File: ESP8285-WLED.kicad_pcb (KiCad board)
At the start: 2 copper layers, 62.2 x 35.6 mm, 56 parts, among them J1 WLED, J2 USB_B_Micro, J3 ANT, Q1 UMH3N, SW1 RESET, SW2 FLASH, U1 ME3116, U2 ESP8285, U3 ME6211, U4 TXS0101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

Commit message: more tweaking
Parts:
- moved C1 2.58 mm to (126.5, 117.1), turned to 270 degrees
- moved R16 2.51 mm to (141.4, 113.5)
- moved C2 2.29 mm to (132.2, 117.2), turned to 270 degrees
- moved Y1 1.19 mm to (129.3, 117.2), turned to 0 degrees
- moved R7 0.59 mm to (127.4, 114.6)
- moved R15 0.34 mm to (141.0, 114.7), turned to 315 degrees
- turned SW1 to 0 degrees
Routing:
- net /RST: track 42.7 -> 34.7 mm, vias 0 -> 2
- net +3V3: track 130.9 -> 137.5 mm
- net GND: track 16.8 -> 12.5 mm, vias 54 -> 58
- net Net-(C15-Pad1): track 4.42 -> 1.99 mm
- net Net-(AE1-Pad1): track 1.86 -> 4.25 mm
- net /XI: track 6.90 -> 5.43 mm
- net /CUTXD: track 19.1 -> 20.5 mm
- net /XO: track 6.88 -> 7.95 mm
- net /UTXD: track 3.43 -> 2.79 mm

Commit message: even more tweaks
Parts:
- moved H1 0.19 mm to (149.3, 123.8)
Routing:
- net Net-(J2-Pad6): track 12.7 -> 19.1 mm
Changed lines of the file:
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@@
     (thickness 1.6)
     (drawings 14)
-    (tracks 441)
+    (tracks 447)
     (zones 0)
     (modules 56)
@@
   )
   (setup
-    (last_trace_width 0.25)
+    (last_trace_width 0.9)
     (user_trace_width 0.35)
     (user_trace_width 0.5)
@@
   )
   (module MountingHole:MountingHole_4mm (layer F.Cu)
-    (at 149.098 123.825)
+    (at 149.2885 123.825)
     (descr "Mounting Hole 4mm, no annular")
     (tags "mounting hole 4mm no annular")
@@
     (effects (font (size 2 2) (thickness 0.3)) (justify left mirror))
   )
-  (gr_text RESET (at 131.2545 123.952) (layer F.Cu)
+  (gr_text RESET (at 131.2545 124.1425) (layer F.Cu)
     (effects (font (size 1 1) (thickness 0.2)))
   )
@@
   (segment (start 113.68 99.456) (end 114.8315 100.6075) (width 0.5) (layer F.Cu) (net 2) (status 20))
   (segment (start 97.79 122.301) (end 97.79 122.301) (width 0.5) (layer F.Cu) (net 2) (status 20))
-  (via (at 145.542 111.252) (size 1.6) (drill 0.9) (layers F.Cu B.Cu) (net 2))
-  (via (at 145.542 108.585) (size 1.6) (drill 0.9) (layers F.Cu B.Cu) (net 2))
-  (via (at 145.542 106.172) (size 1.6) (drill 0.9) (layers F.Cu B.Cu) (net 2))
-  (via (at 145.542 103.632) (size 1.6) (drill 0.9) (layers F.Cu B.Cu) (net 2))
-  (via (at 145.542 100.965) (size 1.6) (drill 0.9) (layers F.Cu B.Cu) (net 2))
-  (via (at 145.542 98.552) (size 1.6) (drill 0.9) (layers F.Cu B.Cu) (net 2))
-  (via (at 145.542 120.396) (size 1.6) (drill 0.9) (layers F.Cu B.Cu) (net 2))
-  (via (at 145.542 122.936) (size 1.6) (drill 0.9) (layers F.Cu B.Cu) (net 2))
-  (via (at 145.542 125.349) (size 1.6) (drill 0.9) (layers F.Cu B.Cu) (net 2))
-  (via (at 145.542 96.012) (size 1.6) (drill 0.9) (layers F.Cu B.Cu) (net 2))
-  (via (at 145.542 93.472) (size 1.6) (drill 0.9) (layers F.Cu B.Cu) (net 2))
-  (via (at 145.542 117.856) (size 1.6) (drill 0.9) (layers F.Cu B.Cu) (net 2))
+  (via (at 145.796 111.252) (size 1.6) (drill 0.9) (layers F.Cu B.Cu) (net 2))
+  (via (at 145.796 108.585) (size 1.6) (drill 0.9) (layers F.Cu B.Cu) (net 2))
+  (via (at 145.796 100.965) (size 1.6) (drill 0.9) (layers F.Cu B.Cu) (net 2))
+  (via (at 145.796 98.552) (size 1.6) (drill 0.9) (layers F.Cu B.Cu) (net 2))
+  (via (at 145.8595 120.396) (size 1.6) (drill 0.9) (layers F.Cu B.Cu) (net 2))
+  (via (at 145.8595 122.936) (size 1.6) (drill 0.9) (layers F.Cu B.Cu) (net 2))
+  (via (at 145.8595 125.349) (size 1.6) (drill 0.9) (layers F.Cu B.Cu) (net 2))
+  (via (at 145.796 96.012) (size 1.6) (drill 0.9) (layers F.Cu B.Cu) (net 2))
+  (via (at 145.796 93.472) (size 1.6) (drill 0.9) (layers F.Cu B.Cu) (net 2))
+  (via (at 145.8595 117.856) (size 1.6) (drill 0.9) (layers F.Cu B.Cu) (net 2))
   (via (at 104.775 94.869) (size 1.6) (drill 0.9) (layers F.Cu B.Cu) (net 2))
   (via (at 102.489 96.266) (size 1.6) (drill 0.9) (layers F.Cu B.Cu) (net 2))
@@
   (via (at 123.5075 109.6645) (size 1.6) (drill 0.9) (layers F.Cu B.Cu) (net 2))
   (via (at 121.412 107.95) (size 1.6) (drill 0.9) (layers F.Cu B.Cu) (net 2))
+  (via (at 145.796 106.172) (size 1.6) (drill 0.9) (layers F.Cu B.Cu) (net 2))
+  (via (at 145.796 103.632) (size 1.6) (drill 0.9) (layers F.Cu B.Cu) (net 2))
   (segment (start 94.488 105.1) (end 92.908 105.1) (width 0.5) (layer B.Cu) (net 3) (status 10))
   (segment (start 92.908 105.1) (end 91.821 104.013) (width 0.5) (layer B.Cu) (net 3))
@@
   (segment (start 140.1445 107.442) (end 139.6365 107.95) (width 0.5) (layer F.Cu) (net 4))
   (segment (start 139.5095 103.465) (end 140.1445 104.1) (width 0.5) (layer F.Cu) (net 4))
-  (segment (start 140.843 102.1315) (end 139.5095 103.465) (width 0.5) (layer F.Cu) (net 4))
-  (segment (start 140.843 97.409) (end 140.843 102.1315) (width 0.5) (layer F.Cu) (net 4))
-  (segment (start 140.335 96.901) (end 140.843 97.409) (width 0.5) (layer F.Cu) (net 4))
-  (segment (start 138.303 97.282) (end 138.684 96.901) (width 0.5) (layer F.Cu) (net 4))
-  (segment (start 138.684 96.901) (end 140.335 96.901) (width 0.5) (layer F.Cu) (net 4))
-  (segment (start 130.556 101.727) (end 135.001 97.282) (width 0.5) (layer F.Cu) (net 4))
-  (segment (start 135.001 97.282) (end 138.303 97.282) (width 0.5) (layer F.Cu) (net 4))
-  (segment (start 130.556 102.696) (end 130.556 101.727) (width 0.5) (layer F.Cu) (net 4))
   (segment (start 138.049 103.505) (end 139.4695 103.505) (width 0.25) (layer F.Cu) (net 4))
   (segment (start 134.747 106.807) (end 138.049 103.505) (width 0.25) (layer F.Cu) (net 4))
@@
   (segment (start 119.6975 116.6495) (end 125.4125 110.9345) (width 0.5) (layer F.Cu) (net 4))
   (segment (start 119.5705 116.6495) (end 119.6975 116.6495) (width 0.5) (layer F.Cu) (net 4))
+  (segment (start 139.6765 103.465) (end 139.5095 103.465) (width 0.5) (layer F.Cu) (net 4))
+  (segment (start 140.716 102.4255) (end 139.6765 103.465) (width 0.5) (layer F.Cu) (net 4))
+  (segment (start 140.716 97.282) (end 140.716 102.4255) (width 0.5) (layer F.Cu) (net 4))
+  (segment (start 140.335 96.901) (end 140.716 97.282) (width 0.5) (layer F.Cu) (net 4))
+  (segment (start 138.684 96.901) (end 140.335 96.901) (width 0.5) (layer F.Cu) (net 4))
+  (segment (start 138.303 97.282) (end 138.684 96.901) (width 0.5) (layer F.Cu) (net 4))
+  (segment (start 135.001 97.282) (end 138.303 97.282) (width 0.5) (layer F.Cu) (net 4))
+  (segment (start 130.556 101.727) (end 135.001 97.282) (width 0.5) (layer F.Cu) (net 4))
+  (segment (start 130.556 102.696) (end 130.556 101.727) (width 0.5) (layer F.Cu) (net 4))
   (segment (start 137.036 107.9) (end 136.986 107.95) (width 0.35) (layer F.Cu) (net 5) (status 30))
   (segment (start 137.036 106.172) (end 137.036 107.9) (width 0.35) (layer F.Cu) (net 5) (status 30))
@@
   (segment (start 90.97 122.471) (end 92.52 124.021) (width 0.5) (layer F.Cu) (net 14) (status 30))
   (segment (start 90.97 122.096) (end 90.97 122.471) (width 0.5) (layer F.Cu) (net 14) (status 30))
+  (segment (start 94 116.771) (end 95.2 117.971) (width 0.9) (layer F.Cu) (net 14))
+  (segment (start 92.52 116.771) (end 94 116.771) (width 0.9) (layer F.Cu) (net 14))
+  (segment (start 95.2 122.821) (end 95.2 122.9225) (width 0.9) (layer F.Cu) (net 14))
+  (segment (start 94.1015 124.021) (end 92.52 124.021) (width 0.9) (layer F.Cu) (net 14))
+  (segment (start 95.2 122.9225) (end 94.1015 124.021) (width 0.9) (layer F.Cu) (net 14))
   (segment (start 141.678735 116.786735) (end 141.756 116.864) (width 0.35) (layer F.Cu) (net 15))
   (segment (start 141.678735 115.326235) (end 141.678735 116.786735) (width 0.35) (layer F.Cu) (net 15))

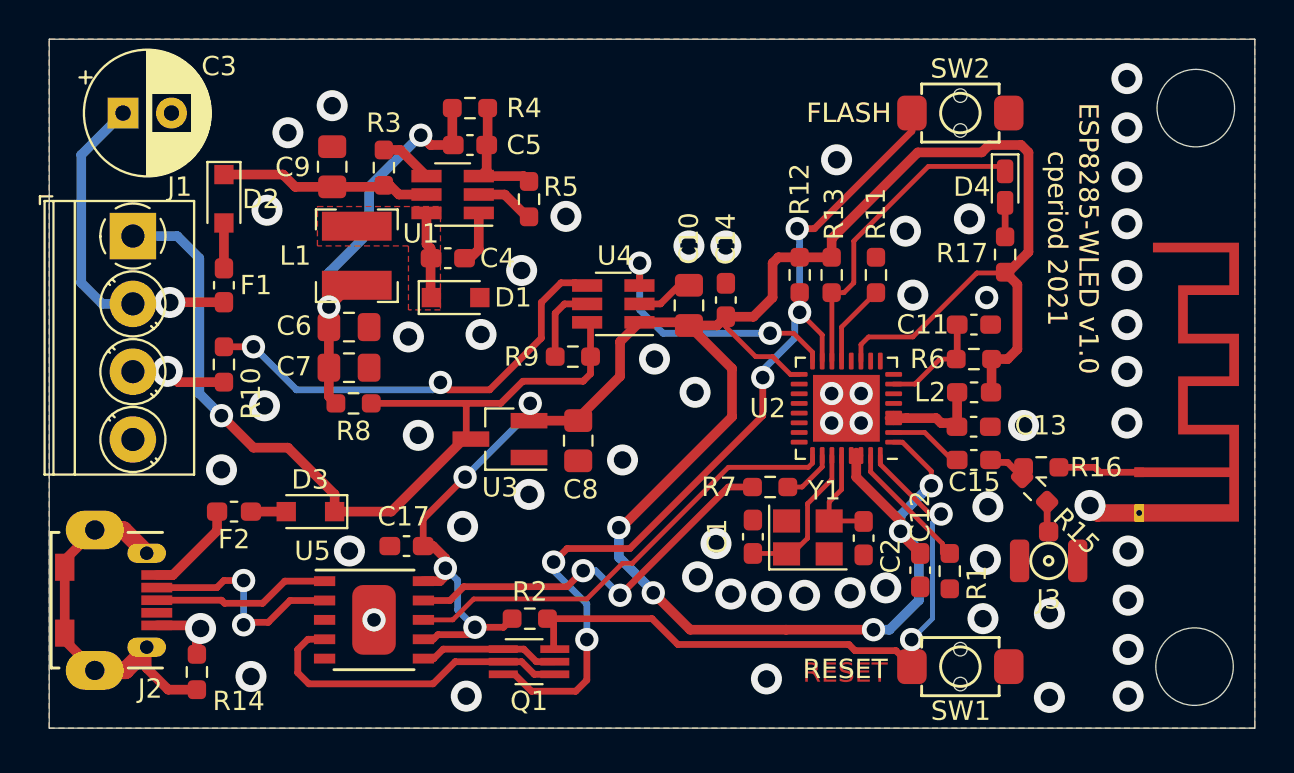
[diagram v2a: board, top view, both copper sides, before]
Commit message: updates and tweaks based on actually building one
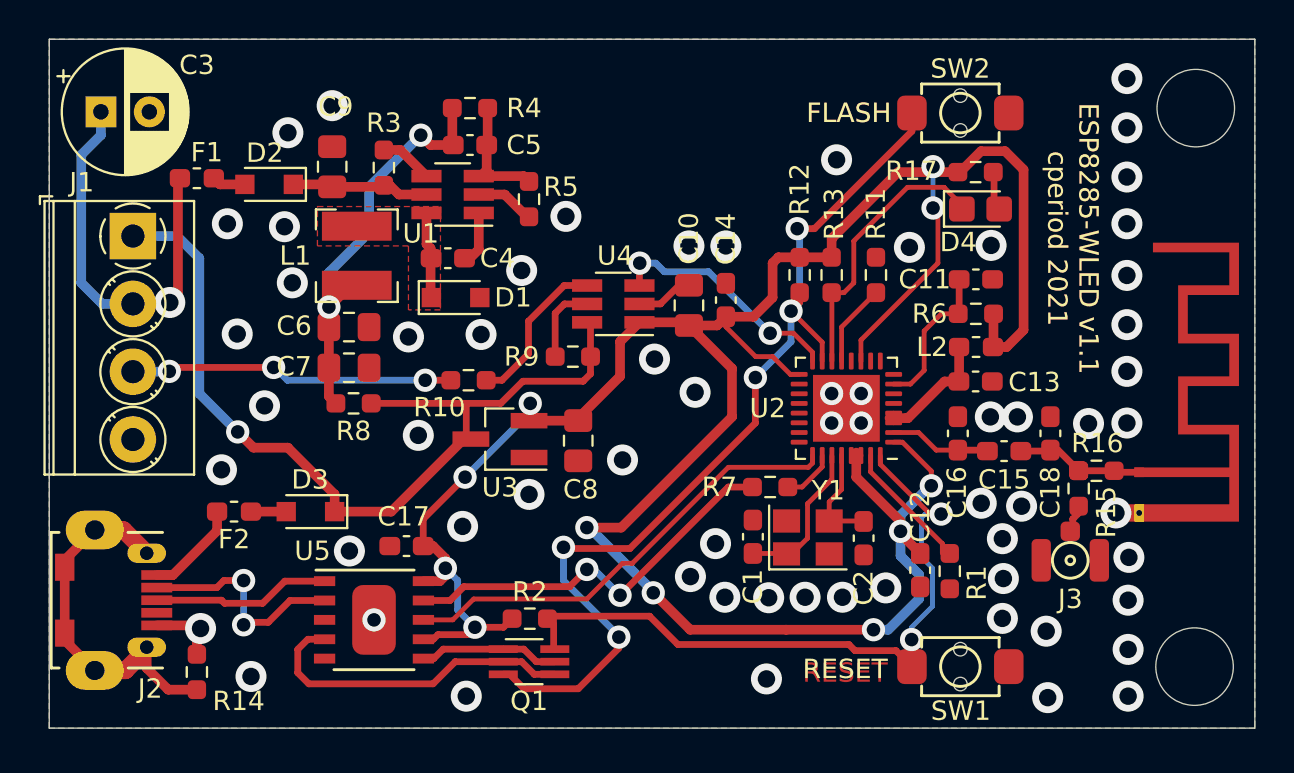
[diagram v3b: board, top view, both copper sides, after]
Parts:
- added C16: DNP, Capacitor_SMD:C_0603_1608Metric_Pad1.08x0.95mm_HandSolder, F.Cu at (137.1, 111.8)
- added C18: DNP, Capacitor_SMD:C_0603_1608Metric_Pad1.08x0.95mm_HandSolder, F.Cu at (141.8, 111.8)
- C1, C2: value 6.8p -> 10p
- C9: value 22u -> 22u 25v
- D4: footprint LED_SMD:LED_0603_1608Metric_Castellated -> LED_SMD:LED_0805_2012Metric_Castellated
- moved R10 12.7 mm to (111.8, 109.0), turned to 0 degrees
- moved F1 5.70 mm to (97.8, 98.6), turned to 0 degrees
- moved R17 4.52 mm to (138.0, 98.3), turned to 180 degrees
- moved R16 2.85 mm to (144.2, 113.7)
- moved D2 2.45 mm to (101.5, 98.9), turned to 180 degrees
- moved L2 2.34 mm to (138.0, 107.3)
- moved C13 2.34 mm to (138.0, 109.1)
- moved C11 2.34 mm to (138.0, 103.8)
- moved R6 2.34 mm to (138.0, 105.6)
- moved R15 2.27 mm to (143.3, 114.6), turned to 90 degrees
- moved D4 1.70 mm to (138.2, 100.2), turned to 0 degrees
- moved C15 1.63 mm to (139.5, 112.7)
- moved C3 1.14 mm to (92.8, 95.2)
- moved J3 1.12 mm to (142.9, 118.3)
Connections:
- R15 pad 1: Net-(C15-Pad1) -> Net-(J3-Pad1)
- R15 pad 2: Net-(J3-Pad1) -> Net-(C15-Pad1)
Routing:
- net Net-(R10-Pad2): track 23.4 -> 8.22 mm, vias 2 -> 0
- net Net-(J1-Pad3): track 4.94 -> 16.8 mm, vias 1 -> 3
- net /12VIN: track 10.9 -> 7.16 mm
- net +12V: track 17.5 -> 20.9 mm
- net Net-(C15-Pad1): track 1.99 -> 5.34 mm
- net Net-(AE1-Pad1): track 4.25 -> 1.33 mm
- net /EN: track 5.56 -> 7.82 mm
- net /GPIO2: track 16.6 -> 14.4 mm
- net +3V3: track 137.5 -> 139.6 mm, vias 9 -> 11
- net GND: track 12.5 -> 11.0 mm, vias 58 -> 63
- net WLED: track 13.9 -> 12.4 mm
- net /GPIO0: track 49.1 -> 50.5 mm
- net /ANT_LNA: track 3.86 -> 5.17 mm
- net /RST: track 34.7 -> 35.8 mm
- net Net-(C13-Pad2): track 6.94 -> 7.71 mm
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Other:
- board text added: "ESP8285-WLED v1.1 cperiod 2021"
- board text removed: "ESP8285-WLED v1.0 cperiod 2021"
